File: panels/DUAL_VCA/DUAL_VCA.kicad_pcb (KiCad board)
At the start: 2 copper layers, 70.8 x 128.4 mm, 15 parts

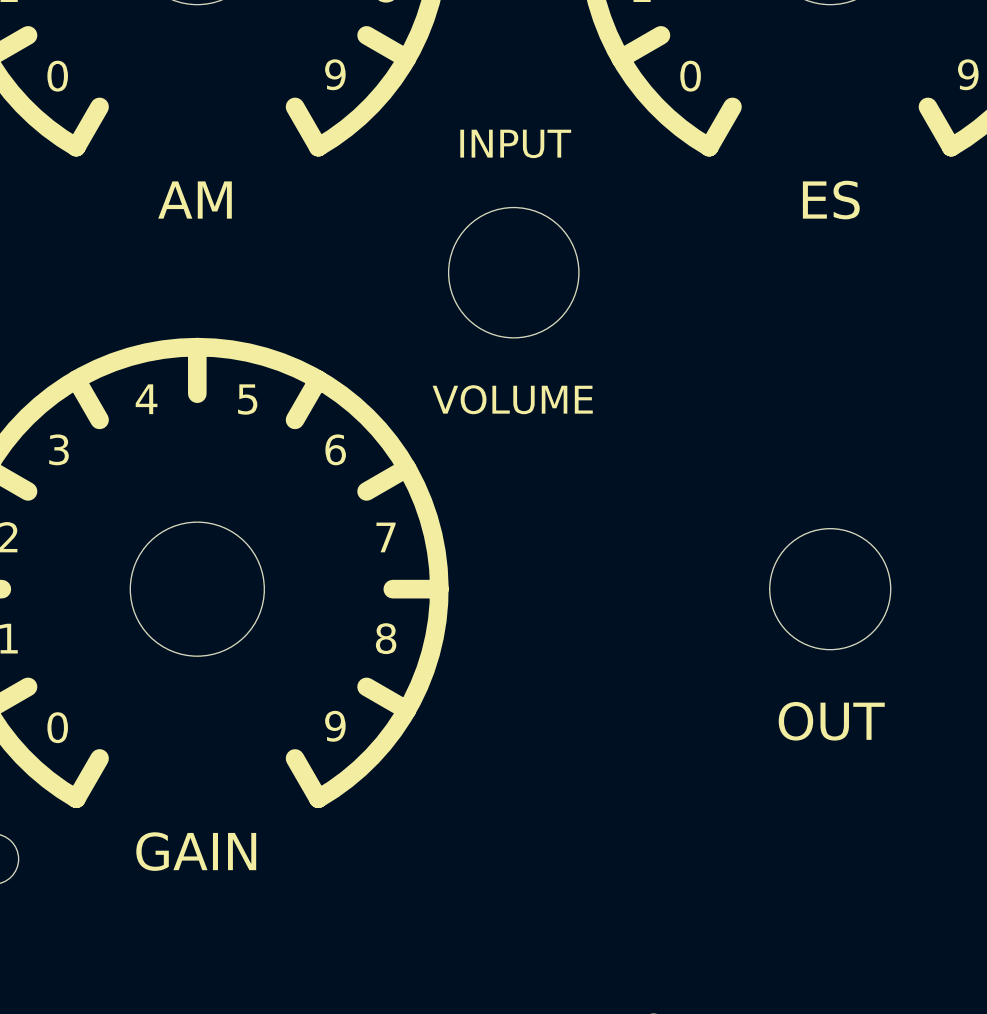
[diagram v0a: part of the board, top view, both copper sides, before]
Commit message: dual vca pcb traces
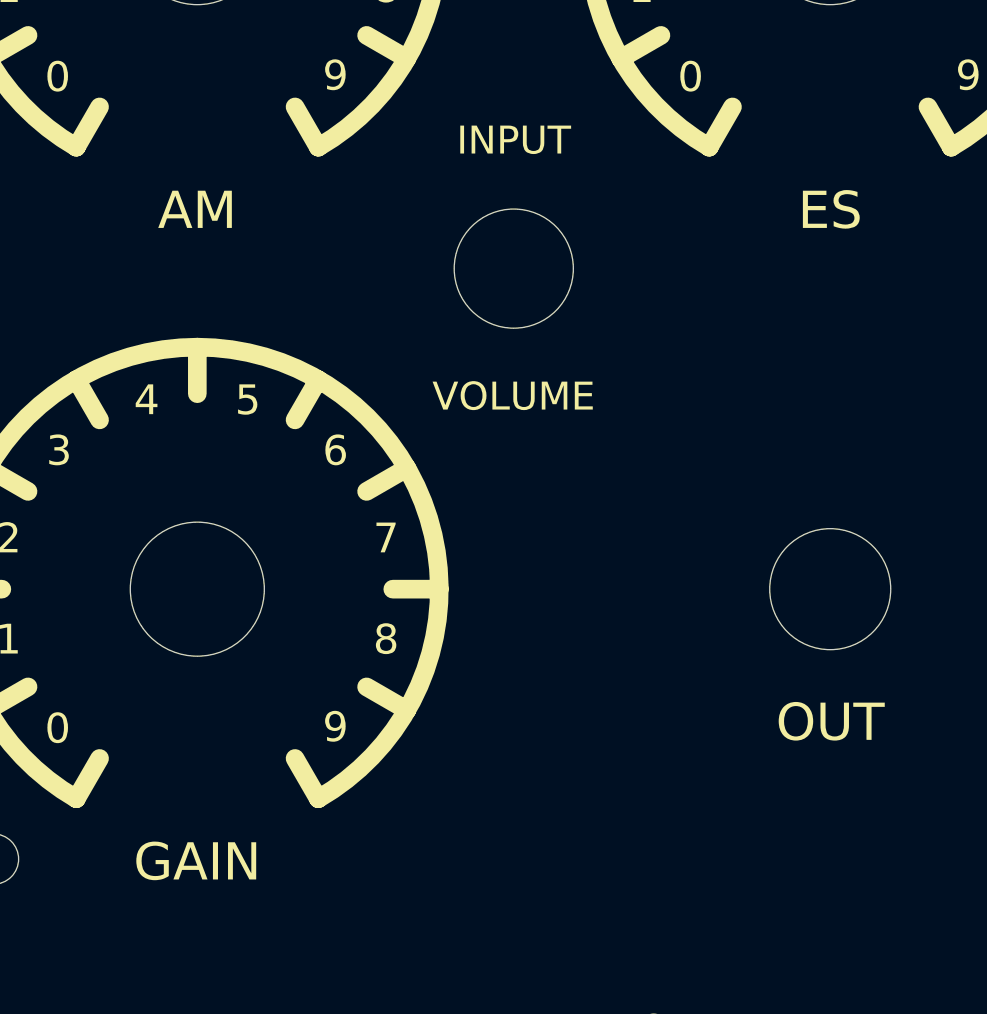
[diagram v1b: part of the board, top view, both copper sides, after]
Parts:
- removed the REF** at (101.6, 121.7)
- added REF**: LED_3mm_6mm_Bezel, FormantKO-Panel:LED_3mm_6mm_Bezel, F.Cu at (101.6, 121.5)

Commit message: finish? dual vca module & panel
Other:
- board text added: "${COMPANY} ${COMMENT4}"
- board text added: "${TITLE} ${COMMENT5} REV ${REVISION} ${ISSUE_DATE}"
- board text removed: "${COMPANY} ${TAG}"
- board text removed: "${MODULE} ${PARTNO} REVISION ${REVISION} ${ISSUE_DATE}"
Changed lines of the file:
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@@
 	(title_block
 		(title "DUAL-VCA")
-		(date "2026-06-12")
+		(date "2026-07-14")
 		(rev "A")
 		(company "THE HOUSE OF GALAHAD")
-		(comment 1 "FORMANT-KO")
+		(comment 1 "FORMANT^{KO}")
+		(comment 2 "mailto:paul.f.burdette@gmail.com")
+		(comment 3 "httpd://github.com/Desval27/FormantKO/")
+		(comment 4 "No Organic Grounding")
+		(comment 5 "9726-F")
 	)
 	(layers
@@
 		)
 	)
-	(property "EMAIL" "mailto:paul.f.burdette@gmail.com")
-	(property "GITHUB" "https://github.com/Desval27/FormantKO/")
-	(property "MODULE" "DUAL-VCA")
-	(property "PARTNO" "9726-F")
-	(property "TAG" "NO ORGANIC GROUNDING")
 	(footprint "FormantKO-Panel:Jack_3.5mm"
 		(layer "F.Cu")
@@
 		)
 	)
-	(gr_text "${COMPANY}\n${TAG}"
+	(gr_text "${COMPANY}\n${COMMENT4}"
 		(at 101.645894 44.515428 0)
 		(layer "B.SilkS")
@@
 		)
 	)
-	(gr_text "${MODULE} ${PARTNO}\nREVISION ${REVISION} ${ISSUE_DATE}"
+	(gr_text "${TITLE} ${COMMENT5}\nREV ${REVISION} ${ISSUE_DATE}"
 		(at 101.635894 164.915428 0)
 		(layer "B.SilkS")

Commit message: com test ready panel & pcb
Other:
- board text added: "${COMMENT1}"
- board text removed: "FORMANT^{KO}"
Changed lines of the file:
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@@
 		)
 	)
-	(gr_text "FORMANT^{KO}"
+	(gr_text "${COMMENT1}"
 		(at 101.635894 162.915428 0)
 		(layer "F.SilkS")
